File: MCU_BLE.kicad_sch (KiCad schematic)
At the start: 40 parts, among them Q1 DMG1012T, Q2 DMG1012T, U1 STM32WB55RGVx, U3 AT25SL321-U, Y1 32MHz, Y2 32.768k

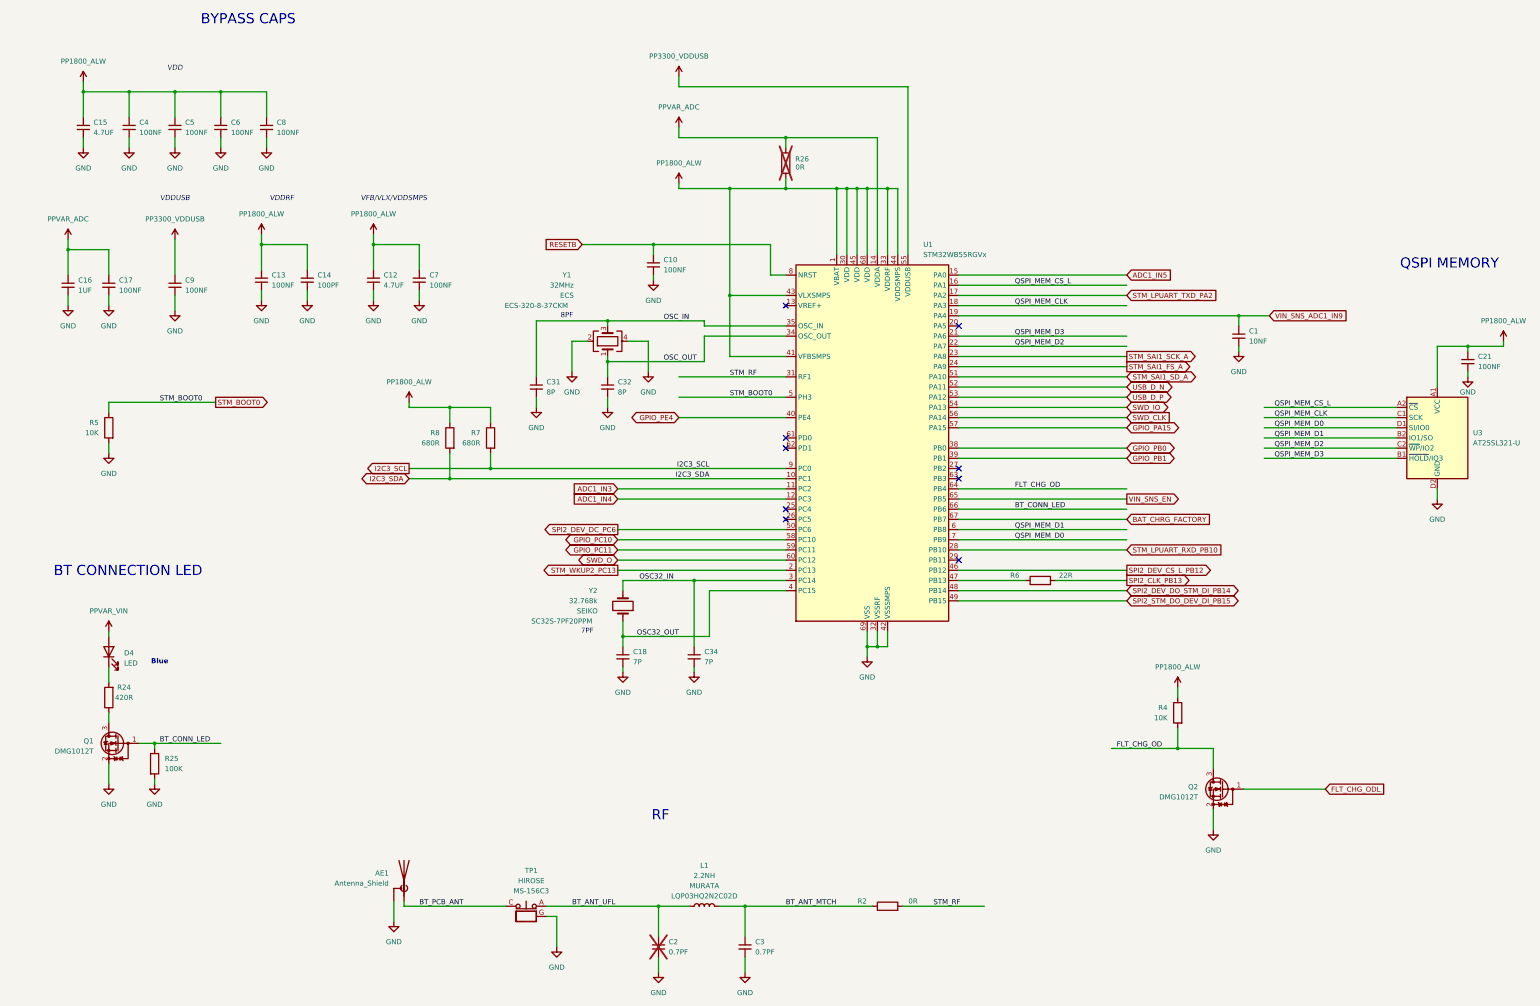
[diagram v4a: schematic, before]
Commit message: Various BOM and Bug Fixes * Changed Stackup to common JLCPCB stackup * Modified trace widths as per new stackup * Reduced drill hole size * Rotated uFL connector as per datasheet pinout * Added pop options for ADC voltage * removed some GPIO and added GND to headers * BOM changes for battery charger, USB connector etc. to support component specifications and USB standards. * Improved MCU bypass and power delivery routing * Various other small bug fixes
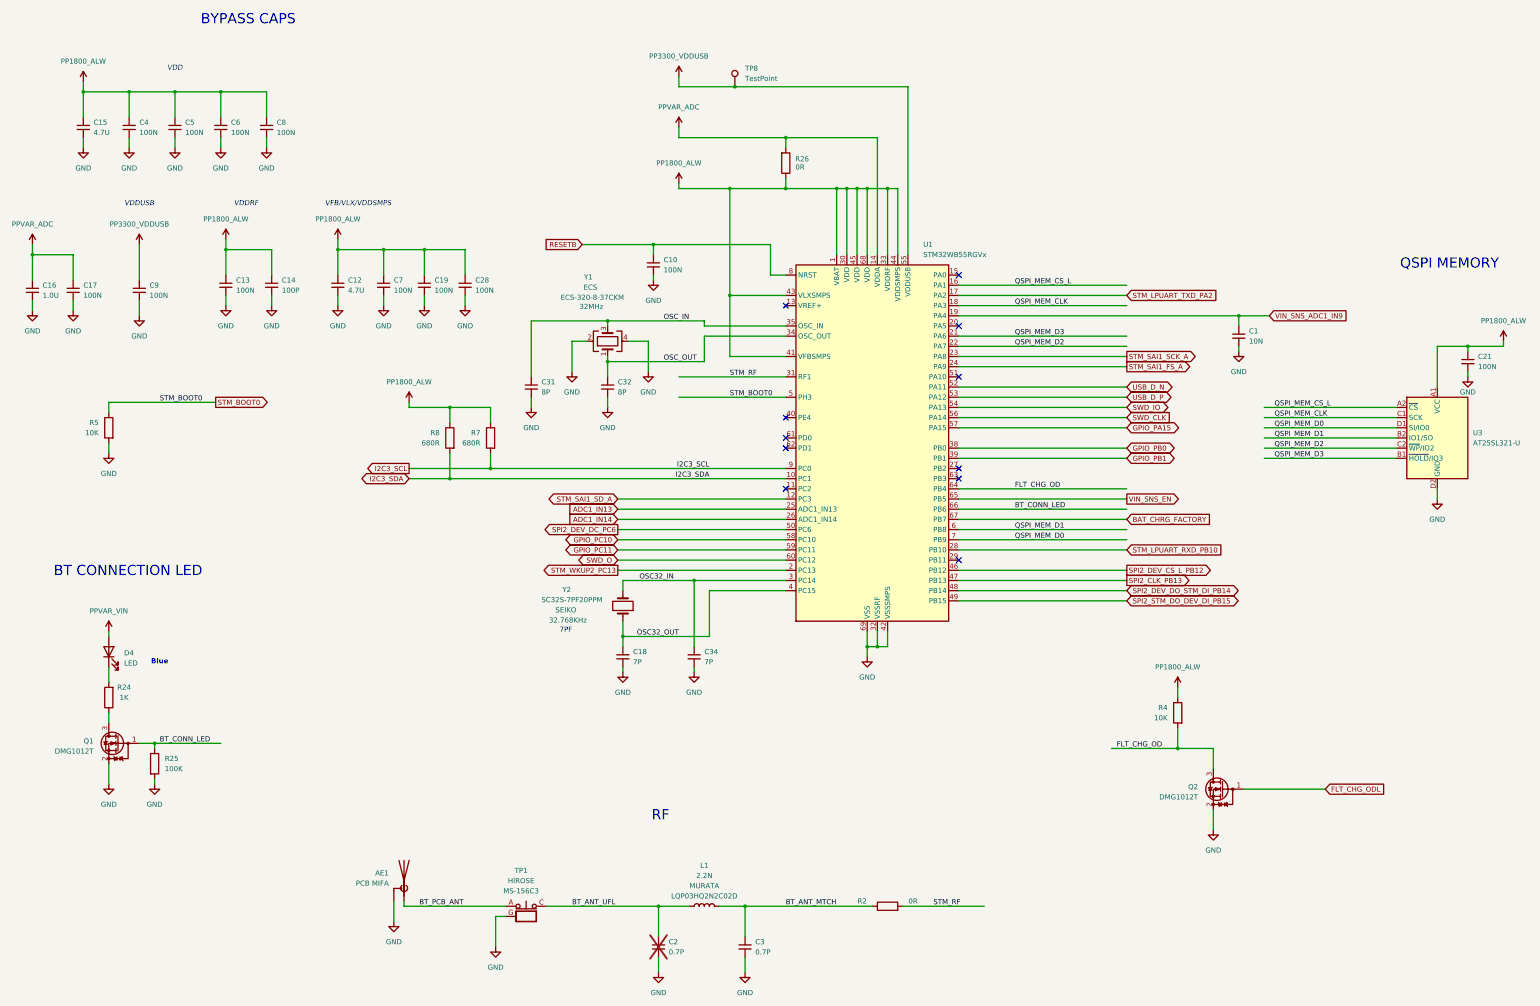
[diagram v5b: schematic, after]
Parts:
- removed R6: 22R, Resistor_SMD:R_0201_0603Metric, symbol Device:R
- added C19, C28: 100N, Capacitor_SMD:C_0201_0603Metric, symbol Device:C_Small
- added TP8: TestPoint, TestPoint:TestPoint_Pad_D1.0mm, symbol Connector:TestPoint
- AE1: value Antenna_Shield -> PCB MIFA
- C1: value 10NF -> 10N
- C10, C13, C17, C21, C4, C5, C6, C7, C8, C9: value 100NF -> 100N
- C12, C15: value 4.7UF -> 4.7U
- C14: value 100PF -> 100P
- C16: value 1UF -> 1.0U
- C2, C3: value 0.7PF -> 0.7P
- L1: value 2.2NH -> 2.2N
- R24: value 420R -> 1K
- R26: now fitted
- Y1: value 32MHz -> ECS-320-8-37CKM; FREQ (none) -> 32MHz
- Y2: value 32.768k -> SC32S-7PF20PPM; FREQ (none) -> 32.768KHz
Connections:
- net ADC1_IN4 is gone; now on net STM_SAI1_SD_A: U1.12 (PC3)
- net BT_ANT_UFL: now also TP1.C; no longer TP1.A
- net BT_PCB_ANT: now also TP1.A; no longer TP1.C
- net GND: now also C19.2, C28.2
- net PP1800_ALW: now also C19.1, C28.1
- net PP3300_VDDUSB: now also TP8.1
- net SPI2_CLK_PB13: now also U1.47 (PB13)
- net STM_SAI1_SD_A: no longer U1.51 (PA10)
- net ADC1_IN13: now reaches U1.25 (PC4)
- net ADC1_IN14: now reaches U1.26 (PC5)
- net ADC1_IN3: no longer names the net of U1.11 (PC2)
- net ADC1_IN5: no longer names the net of U1.15 (PA0)
- net GPIO_PE4: no longer names the net of U1.40 (PE4)
- no-connect marks 9 -> 11
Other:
- note removed: "8PF"
- moved on the sheet: C12, C13, C14, C16, C17, C31, C7, C9
